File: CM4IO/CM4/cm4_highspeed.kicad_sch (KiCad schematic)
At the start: 1 part

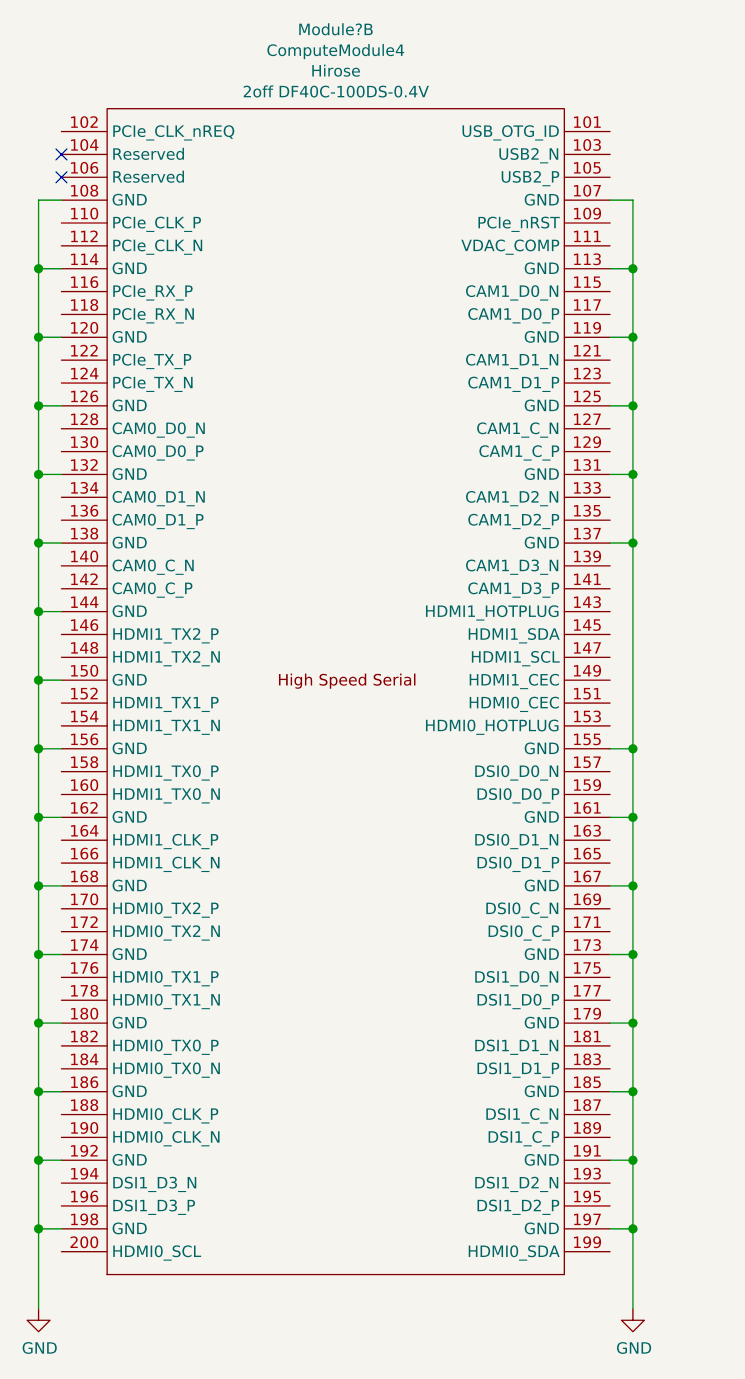
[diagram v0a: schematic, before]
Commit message: Initial CM4IO board design
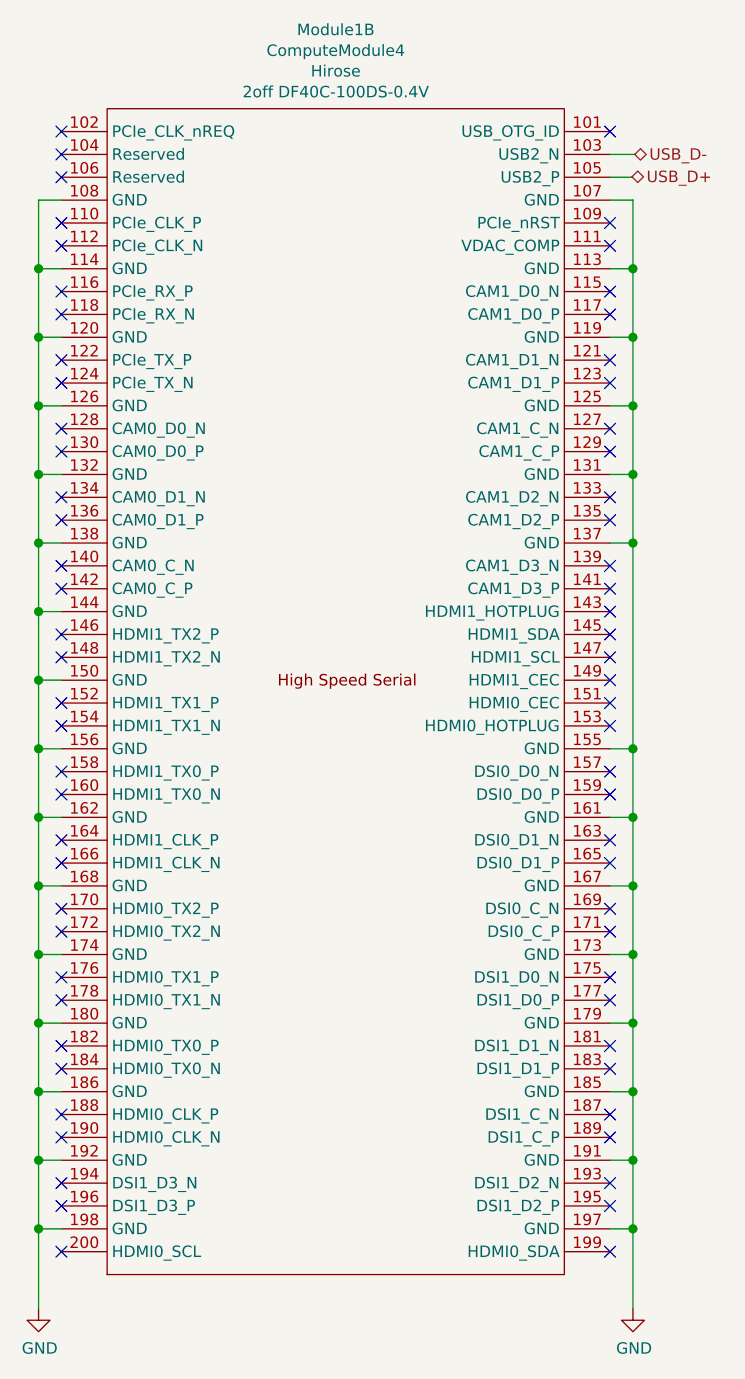
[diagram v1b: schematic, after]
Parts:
- gave numbers to parts that had none: 1
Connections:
- net USB_D-: now reaches Module1.103 (USB2_N)
- net USB_D+: now reaches Module1.105 (USB2_P)
- no-connect marks 2 -> 68
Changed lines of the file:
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@@
   (junction (at 124.968 145.0848) (diameter 1.016) (color 0 0 0 0))
   (junction (at 124.968 152.7048) (diameter 1.016) (color 0 0 0 0))
+  (no_connect (at 61.468 147.6248))
+  (no_connect (at 122.428 51.1048))
+  (no_connect (at 61.468 112.0648))
+  (no_connect (at 61.468 150.1648))
+  (no_connect (at 61.468 66.3448))
+  (no_connect (at 61.468 140.0048))
+  (no_connect (at 122.428 81.5848))
+  (no_connect (at 122.428 147.6248))
+  (no_connect (at 61.468 81.5848))
+  (no_connect (at 122.428 94.2848))
+  (no_connect (at 61.468 30.7848))
+  (no_connect (at 61.468 56.1848))
+  (no_connect (at 61.468 124.7648))
+  (no_connect (at 122.428 112.0648))
+  (no_connect (at 61.468 96.8248))
+  (no_connect (at 61.468 142.5448))
+  (no_connect (at 122.428 71.4248))
+  (no_connect (at 122.428 58.7248))
+  (no_connect (at 122.428 140.0048))
+  (no_connect (at 122.428 150.1648))
+  (no_connect (at 122.428 142.5448))
+  (no_connect (at 61.468 51.1048))
+  (no_connect (at 122.428 96.8248))
+  (no_connect (at 122.428 134.9248))
+  (no_connect (at 61.468 73.9648))
+  (no_connect (at 61.468 94.2848))
+  (no_connect (at 122.428 117.1448))
+  (no_connect (at 61.468 104.4448))
+  (no_connect (at 122.428 40.9448))
+  (no_connect (at 61.468 35.8648))
+  (no_connect (at 61.468 63.8048))
+  (no_connect (at 122.428 127.3048))
+  (no_connect (at 122.428 119.6848))
+  (no_connect (at 61.468 48.5648))
+  (no_connect (at 61.468 127.3048))
+  (no_connect (at 122.428 109.5248))
+  (no_connect (at 122.428 79.0448))
+  (no_connect (at 122.428 104.4448))
+  (no_connect (at 122.428 43.4848))
+  (no_connect (at 61.468 119.6848))
+  (no_connect (at 61.468 86.6648))
+  (no_connect (at 122.428 101.9048))
+  (no_connect (at 122.428 124.7648))
+  (no_connect (at 122.428 30.7848))
   (no_connect (at 61.468 33.3248))
-  (no_connect (at 61.468 35.8648))
+  (no_connect (at 61.468 58.7248))
+  (no_connect (at 61.468 89.2048))
+  (no_connect (at 61.468 134.9248))
+  (no_connect (at 61.468 101.9048))
+  (no_connect (at 122.428 84.1248))
+  (no_connect (at 122.428 56.1848))
+  (no_connect (at 122.428 66.3448))
+  (no_connect (at 122.428 63.8048))
+  (no_connect (at 122.428 155.2448))
+  (no_connect (at 61.468 79.0448))
+  (no_connect (at 122.428 91.7448))
+  (no_connect (at 61.468 109.5248))
+  (no_connect (at 61.468 132.3848))
+  (no_connect (at 122.428 89.2048))
+  (no_connect (at 61.468 40.9448))
+  (no_connect (at 122.428 132.3848))
+  (no_connect (at 61.468 43.4848))
+  (no_connect (at 122.428 86.6648))
+  (no_connect (at 61.468 117.1448))
+  (no_connect (at 122.428 48.5648))
+  (no_connect (at 61.468 155.2448))
+  (no_connect (at 61.468 71.4248))
+  (no_connect (at 122.428 73.9648))
   (wire (pts (xy 58.928 38.4048) (xy 58.928 46.0248))
     (stroke (width 0) (type solid) (color 0 0 0 0))
@@
     (stroke (width 0) (type solid) (color 0 0 0 0))
   )
+  (wire (pts (xy 122.428 33.3248) (xy 125.1712 33.3248))
+    (stroke (width 0) (type solid) (color 0 0 0 0))
+  )
+  (wire (pts (xy 122.428 35.8648) (xy 124.8664 35.8648))
+    (stroke (width 0) (type solid) (color 0 0 0 0))
+  )
   (wire (pts (xy 122.428 46.0248) (xy 124.968 46.0248))
     (stroke (width 0) (type solid) (color 0 0 0 0))
@@
     (stroke (width 0) (type solid) (color 0 0 0 0))
   )
+  (wire (pts (xy 124.8664 35.8648) (xy 124.8664 35.814))
+    (stroke (width 0) (type solid) (color 0 0 0 0))
+  )
   (wire (pts (xy 124.968 38.4048) (xy 122.428 38.4048))
     (stroke (width 0) (type solid) (color 0 0 0 0))
@@
   (wire (pts (xy 124.968 152.7048) (xy 124.968 161.5948))
     (stroke (width 0) (type solid) (color 0 0 0 0))
+  )
+  (hierarchical_label "USB_D+" (shape bidirectional) (at 124.8664 35.814 0)
+    (effects (font (size 1.27 1.27)) (justify left))
+  )
+  (hierarchical_label "USB_D-" (shape bidirectional) (at 125.1712 33.3248 0)
+    (effects (font (size 1.27 1.27)) (justify left))
   )
   (symbol (lib_id "power:GND") (at 58.928 161.5948 0) (unit 1)
     (in_bom yes) (on_board yes)
-    (property "Reference" "#PWR?" (id 0) (at 58.928 167.9448 0)
+    (property "Reference" "#PWR023" (id 0) (at 58.928 167.9448 0)
       (effects (font (size 1.27 1.27)) hide)
     )
@@
   (symbol (lib_id "power:GND") (at 124.968 161.5948 0) (unit 1)
     (in_bom yes) (on_board yes)
-    (property "Reference" "#PWR?" (id 0) (at 124.968 167.9448 0)
+    (property "Reference" "#PWR024" (id 0) (at 124.968 167.9448 0)
       (effects (font (size 1.27 1.27)) hide)
     )
@@
   (symbol (lib_id "CM4IO:ComputeModule4-CM4") (at -47.752 91.7448 0) (unit 2)
     (in_bom yes) (on_board yes)
-    (property "Reference" "Module?" (id 0) (at 91.948 19.4818 0))
+    (property "Reference" "Module1" (id 0) (at 91.948 19.4818 0))
     (property "Value" "ComputeModule4" (id 1) (at 91.948 21.7932 0))
     (property "Footprint" "CM4IO:Raspberry-Pi-4-Compute-Module" (id 2) (at 94.488 118.4148 0)
